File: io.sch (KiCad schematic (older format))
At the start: 13 parts, among them J5 USB_C_Receptacle_USB2.0, J6 Conn_ARM_JTAG_SWD_10, J7 UART, J8 Conn_02x14_Odd_Even

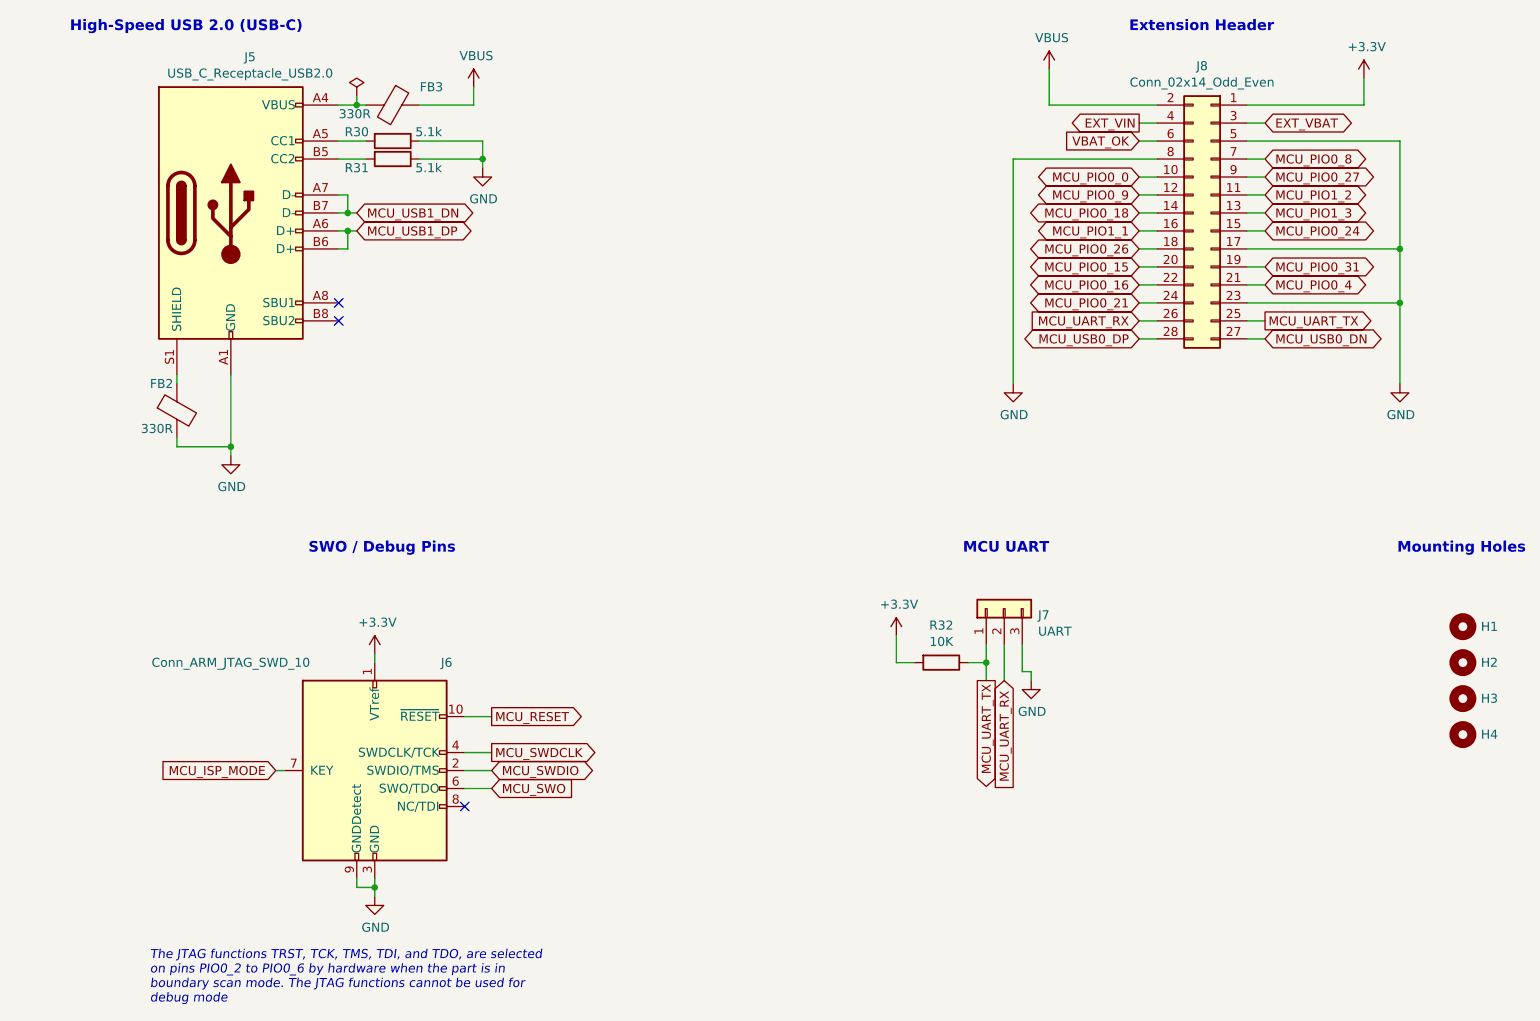
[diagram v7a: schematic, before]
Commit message: Major change of the layout (reviewed) for V1.1
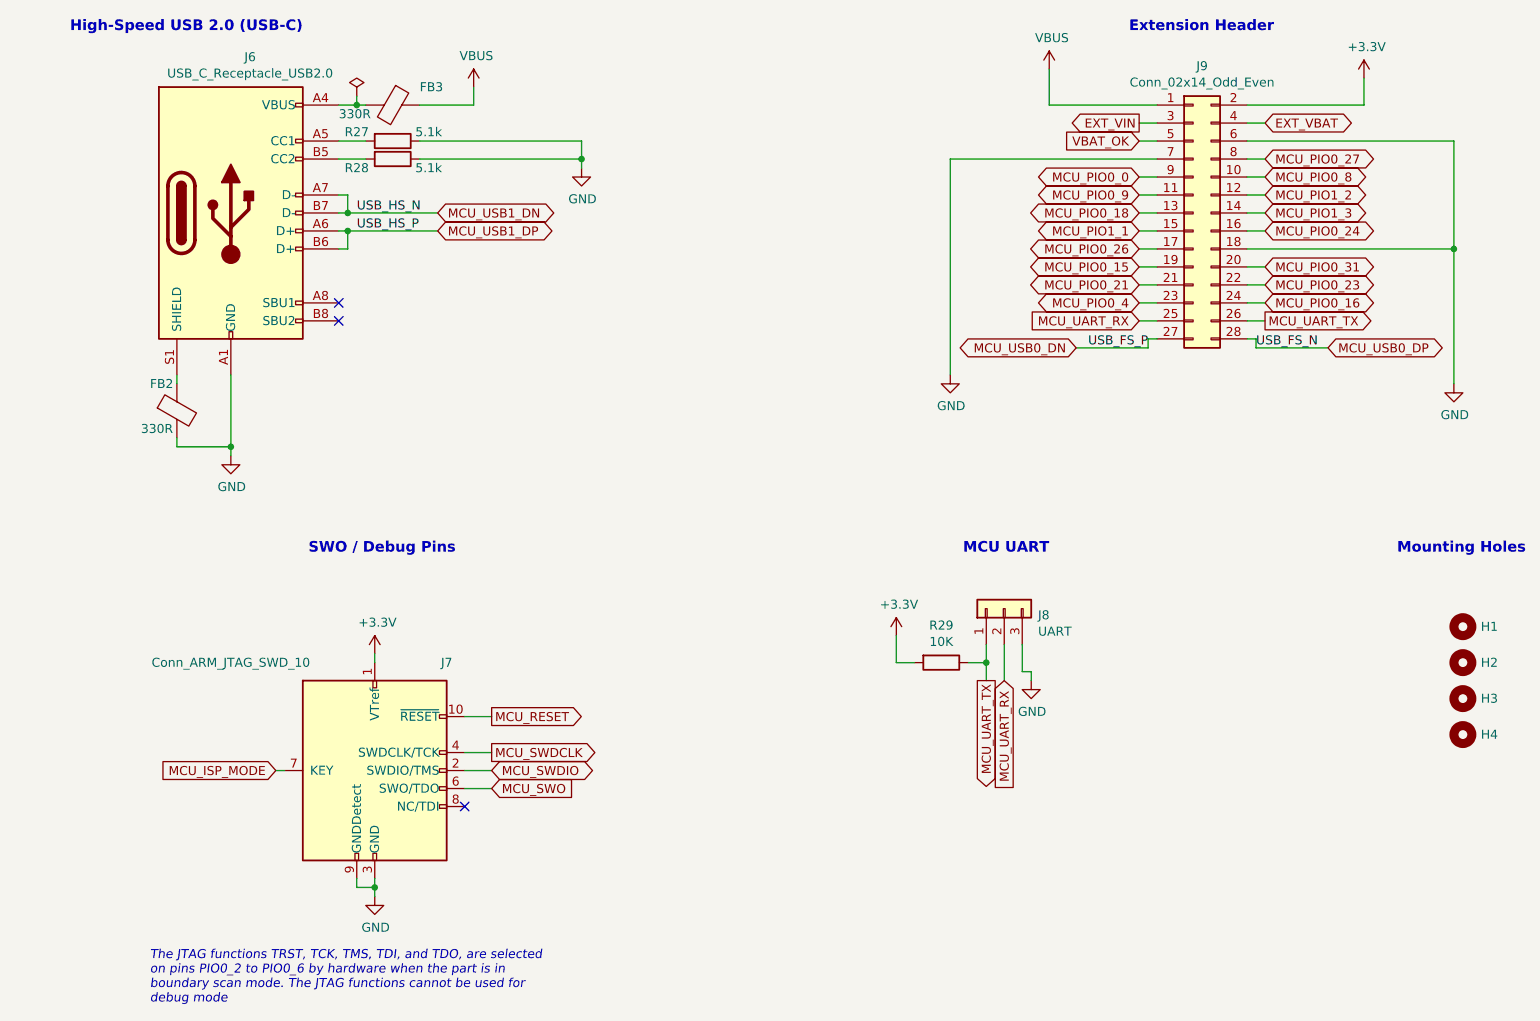
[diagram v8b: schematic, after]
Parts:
- renumbered J5 to J6, J6 to J7, J7 to J8, J8 to J9, R30 to R27, R31 to R28, R32 to R29
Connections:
- net +3V3: now also J9.2 (Pin_2); no longer J9.1 (Pin_1)
- net EXT_VBAT: now also J9.4 (Pin_4); no longer J9.3 (Pin_3)
- net EXT_VIN: now also J9.3 (Pin_3); no longer J9.4 (Pin_4)
- net GND: now also J9.18 (Pin_18), J9.6 (Pin_6), J9.7 (Pin_7); no longer J9.17 (Pin_17), J9.23 (Pin_23), J9.5 (Pin_5), J9.8 (Pin_8)
- net MCU_PIO0_0: now also J9.9 (Pin_9); no longer J9.10 (Pin_10)
- net MCU_PIO0_15: now also J9.19 (Pin_19); no longer J9.20 (Pin_20)
- net MCU_PIO0_16: now also J9.24 (Pin_24); no longer J9.22 (Pin_22)
- net MCU_PIO0_18: now also J9.13 (Pin_13); no longer J9.14 (Pin_14)
- net MCU_PIO0_21: now also J9.21 (Pin_21); no longer J9.24 (Pin_24)
- net MCU_PIO0_24: now also J9.16 (Pin_16); no longer J9.15 (Pin_15)
- net MCU_PIO0_26: now also J9.17 (Pin_17); no longer J9.18 (Pin_18)
- net MCU_PIO0_27: now also J9.8 (Pin_8); no longer J9.9 (Pin_9)
- net MCU_PIO0_31: now also J9.20 (Pin_20); no longer J9.19 (Pin_19)
- net MCU_PIO0_4: now also J9.23 (Pin_23); no longer J9.21 (Pin_21)
- net MCU_PIO0_8: now also J9.10 (Pin_10); no longer J9.7 (Pin_7)
- net MCU_PIO0_9: now also J9.11 (Pin_11); no longer J9.12 (Pin_12)
- net MCU_PIO1_1: now also J9.15 (Pin_15); no longer J9.16 (Pin_16)
- net MCU_PIO1_2: now also J9.12 (Pin_12); no longer J9.11 (Pin_11)
- net MCU_PIO1_3: now also J9.14 (Pin_14); no longer J9.13 (Pin_13)
- net MCU_UART_RX: now also J9.25 (Pin_25); no longer J9.26 (Pin_26)
- net MCU_UART_TX: now also J9.26 (Pin_26); no longer J9.25 (Pin_25)
- net VBAT_OK: now also J9.5 (Pin_5); no longer J9.6 (Pin_6)
- net VBUS: now also J9.1 (Pin_1); no longer J9.2 (Pin_2)
- new net MCU_PIO0_23: J9.22 (Pin_22)
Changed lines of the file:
@@
 Comment4 ""
 $EndDescr
-Text GLabel 3350 2200 2    50   BiDi ~ 0
+Text GLabel 3800 2200 2    50   BiDi ~ 0
 MCU_USB1_DN
 $Comp
-L Connector:USB_C_Receptacle_USB2.0 J5
+L Connector:USB_C_Receptacle_USB2.0 J6
 U 1 1 5F8BDC65
 P 2650 2200
-F 0 "J5" H 2757 3067 50  0000 C CNN
+F 0 "J6" H 2757 3067 50  0000 C CNN
 F 1 "USB_C_Receptacle_USB2.0" H 2757 2976 50  0000 C CNN
 F 2 "tardigrade-components:USB_C_Receptacle_JAE_DX07S016JA1" H 2800 2200 50  0001 C CNN
@@
 	1    0    0    -1
 $EndComp
-Text GLabel 3350 2300 2    50   BiDi ~ 0
+Text GLabel 3800 2300 2    50   BiDi ~ 0
 MCU_USB1_DP
 $Comp
@@
 	2350 3100 2350 3150
 $Comp
-L power:GND #PWR066
+L power:GND #PWR064
 U 1 1 5F8C3DD9
 P 2650 3550
-F 0 "#PWR066" H 2650 3300 50  0001 C CNN
+F 0 "#PWR064" H 2650 3300 50  0001 C CNN
 F 1 "GND" H 2655 3377 50  0000 C CNN
 F 2 "" H 2650 3550 50  0001 C CNN
@@
 NoConn ~ 3250 2800
 $Comp
-L Device:R R31
+L Device:R R28
 U 1 1 5F8C970D
 P 3550 1900
-F 0 "R31" V 3600 1700 50  0000 C CNN
+F 0 "R28" V 3600 1700 50  0000 C CNN
 F 1 "5.1k" V 3600 2100 50  0000 C CNN
 F 2 "Resistor_SMD:R_0402_1005Metric" V 3480 1900 50  0001 C CNN
@@
 $EndComp
 $Comp
-L Device:R R30
+L Device:R R27
 U 1 1 5F8CA21C
 P 3550 1800
-F 0 "R30" V 3500 1600 50  0000 C CNN
+F 0 "R27" V 3500 1600 50  0000 C CNN
 F 1 "5.1k" V 3500 2000 50  0000 C CNN
 F 2 "Resistor_SMD:R_0402_1005Metric" V 3480 1800 50  0001 C CNN
@@
 	3250 1900 3400 1900
 $Comp
-L power:GND #PWR070
+L power:GND #PWR068
 U 1 1 5F8CB237
-P 4050 1950
-F 0 "#PWR070" H 4050 1700 50  0001 C CNN
-F 1 "GND" H 4055 1777 50  0000 C CNN
-F 2 "" H 4050 1950 50  0001 C CNN
-F 3 "" H 4050 1950 50  0001 C CNN
-	1    4050 1950
-	1    0    0    -1
-$EndComp
-Wire Wire Line
-	3700 1900 4050 1900
-Wire Wire Line
-	4050 1900 4050 1950
-Wire Wire Line
-	3700 1800 4050 1800
-Wire Wire Line
-	4050 1800 4050 1900
-Connection ~ 4050 1900
-$Comp
-L power:VBUS #PWR069
+P 4600 1950
+F 0 "#PWR068" H 4600 1700 50  0001 C CNN
+F 1 "GND" H 4605 1777 50  0000 C CNN
+F 2 "" H 4600 1950 50  0001 C CNN
+F 3 "" H 4600 1950 50  0001 C CNN
+	1    4600 1950
+	1    0    0    -1
+$EndComp
+Wire Wire Line
+	3700 1900 4600 1900
+Wire Wire Line
+	4600 1900 4600 1950
+Wire Wire Line
+	3700 1800 4600 1800
+Wire Wire Line
+	4600 1800 4600 1900
+Connection ~ 4600 1900
+$Comp
+L power:VBUS #PWR067
 U 1 1 5F8C64F0
 P 4000 1500
-F 0 "#PWR069" H 4000 1350 50  0001 C CNN
+F 0 "#PWR067" H 4000 1350 50  0001 C CNN
 F 1 "VBUS" H 4015 1673 50  0000 C CNN
 F 2 "" H 4000 1500 50  0001 C CNN
@@
 NoConn ~ 3950 5500
 $Comp
-L power:GND #PWR068
+L power:GND #PWR066
 U 1 1 5FB23809
 P 3450 6000
-F 0 "#PWR068" H 3450 5750 50  0001 C CNN
+F 0 "#PWR066" H 3450 5750 50  0001 C CNN
 F 1 "GND" H 3455 5827 50  0000 C CNN
 F 2 "" H 3450 6000 50  0001 C CNN
@@
 	3450 6000 3450 5950
 $Comp
-L tardigrade-components:Conn_ARM_JTAG_SWD_10 J6
+L tardigrade-components:Conn_ARM_JTAG_SWD_10 J7
 U 1 1 5FB2D29C
 P 3450 5300
-F 0 "J6" H 3850 5900 50  0000 C CNN
+F 0 "J7" H 3850 5900 50  0000 C CNN
 F 1 "Conn_ARM_JTAG_SWD_10" H 2650 5900 50  0000 C CNN
 F 2 "Connector_PinHeader_1.27mm:PinHeader_2x05_P1.27mm_Vertical" H 3450 5300 50  0001 C CNN
@@
 High-Speed USB 2.0 (USB-C)
 $Comp
-L Connector_Generic:Conn_01x03 J7
+L Connector_Generic:Conn_01x03 J8
 U 1 1 5F876392
 P 6950 4400
-F 0 "J7" V 6914 4212 50  0000 R CNN
+F 0 "J8" V 6914 4212 50  0000 R CNN
 F 1 "UART" V 6823 4212 50  0000 R CNN
 F 2 "Connector_PinHeader_2.54mm:PinHeader_1x03_P2.54mm_Vertical" H 6950 4400 50  0001 C CNN
@@
 MCU_UART_TX
 $Comp
-L power:GND #PWR073
+L power:GND #PWR071
 U 1 1 5F877DE3
 P 7100 4800
-F 0 "#PWR073" H 7100 4550 50  0001 C CNN
+F 0 "#PWR071" H 7100 4550 50  0001 C CNN
 F 1 "GND" H 7105 4627 50  0000 C CNN
 F 2 "" H 7100 4800 50  0001 C CNN
@@
 	7100 4750 7100 4800
 $Comp
-L power:+3.3V #PWR071
+L power:+3.3V #PWR069
 U 1 1 5F8E0D6F
 P 6350 4550
-F 0 "#PWR071" H 6350 4400 50  0001 C CNN
+F 0 "#PWR069" H 6350 4400 50  0001 C CNN
 F 1 "+3.3V" H 6365 4723 50  0000 C CNN
 F 2 "" H 6350 4550 50  0001 C CNN
@@
 $EndComp
 $Comp
-L Device:R R32
+L Device:R R29
 U 1 1 5F8E1A3D
 P 6600 4700
-F 0 "R32" V 6393 4700 50  0000 C CNN
+F 0 "R29" V 6393 4700 50  0000 C CNN
 F 1 "10K" V 6484 4700 50  0000 C CNN
 F 2 "Resistor_SMD:R_0402_1005Metric" V 6530 4700 50  0001 C CNN
@@
 	3250 2300 3300 2300
 $Comp
-L power:+3.3V #PWR067
+L power:+3.3V #PWR065
 U 1 1 5F833987
 P 3450 4650
-F 0 "#PWR067" H 3450 4500 50  0001 C CNN
+F 0 "#PWR065" H 3450 4500 50  0001 C CNN
 F 1 "+3.3V" H 3465 4823 50  0000 C CNN
 F 2 "" H 3450 4650 50  0001 C CNN
@@
 Connection ~ 3300 2200
 Wire Wire Line
-	3300 2200 3350 2200
+	3300 2200 3800 2200
 Wire Wire Line
 	3300 2400 3300 2300
 Connection ~ 3300 2300
 Wire Wire Line
-	3300 2300 3350 2300
+	3300 2300 3800 2300
 Wire Wire Line
 	3700 1600 4000 1600
@@
 	3350 1600 3350 1550
 $Comp
-L power:PWR_FLAG #FLG08
+L power:PWR_FLAG #FLG06
 U 1 1 5FCB5DBF
 P 3350 1550
-F 0 "#FLG08" H 3350 1625 50  0001 C CNN
+F 0 "#FLG06" H 3350 1625 50  0001 C CNN
 F 1 "PWR_FLAG" H 3350 1723 50  0001 C CNN
 F 2 "" H 3350 1550 50  0001 C CNN
@@
 Wire Wire Line
 	3450 4650 3450 4700
-$Comp
-L Connector_Generic:Conn_02x14_Odd_Even J8
-U 1 1 5FAF0C03
-P 8100 2200
-F 0 "J8" H 8150 3017 50  0000 C CNN
-F 1 "Conn_02x14_Odd_Even" H 8150 2926 50  0000 C CNN
-F 2 "Connector_PinHeader_2.54mm:PinHeader_2x14_P2.54mm_Vertical" H 8100 2200 50  0001 C CNN
-F 3 "~" H 8100 2200 50  0001 C CNN
-	1    8100 2200
-	-1   0    0    -1
-$EndComp
 Text GLabel 8400 1700 2    50   BiDi ~ 0
 EXT_VBAT
@@
 VBAT_OK
 $Comp
-L power:VBUS #PWR0110
+L power:VBUS #PWR072
 U 1 1 5FB21530
 P 7200 1400
-F 0 "#PWR0110" H 7200 1250 50  0001 C CNN
+F 0 "#PWR072" H 7200 1250 50  0001 C CNN
 F 1 "VBUS" H 7215 1573 50  0000 C CNN
 F 2 "" H 7200 1400 50  0001 C CNN
@@
 	7200 1600 7800 1600
 $Comp
-L power:+3.3V #PWR0111
+L power:+3.3V #PWR073
 U 1 1 5FB24107
 P 8950 1450
-F 0 "#PWR0111" H 8950 1300 50  0001 C CNN
+F 0 "#PWR073" H 8950 1300 50  0001 C CNN
 F 1 "+3.3V" H 8965 1623 50  0000 C CNN
 F 2 "" H 8950 1450 50  0001 C CNN
@@
 $EndComp
 Wire Wire Line
-	8300 1600 8950 1600
-Wire Wire Line
 	8950 1600 8950 1450
-Text GLabel 8400 2900 2    50   BiDi ~ 0
+Text GLabel 7350 2950 0    50   BiDi ~ 0
 MCU_USB0_DN
-Text GLabel 7700 2900 0    50   BiDi ~ 0
+Text GLabel 8750 2950 2    50   BiDi ~ 0
 MCU_USB0_DP
 Text GLabel 8400 2800 2    50   Output ~ 0
@@
 Text GLabel 7700 2800 0    50   Input ~ 0
 MCU_UART_RX
-Text GLabel 8400 2600 2    50   BiDi ~ 0
+Text GLabel 7700 2700 0    50   BiDi ~ 0
 MCU_PIO0_4
-Text GLabel 7700 2700 0    50   BiDi ~ 0
+Text GLabel 7700 2600 0    50   BiDi ~ 0
 MCU_PIO0_21
-Text GLabel 7700 2600 0    50   BiDi ~ 0
+Text GLabel 8400 2700 2    50   BiDi ~ 0
 MCU_PIO0_16
 Text GLabel 7700 2500 0    50   BiDi ~ 0
@@
 Text GLabel 7700 2000 0    50   BiDi ~ 0
 MCU_PIO0_0
+Text GLabel 8400 2000 2    50   BiDi ~ 0
+MCU_PIO0_8
 Text GLabel 8400 1900 2    50   BiDi ~ 0
-MCU_PIO0_8
-Text GLabel 8400 2000 2    50   BiDi ~ 0
 MCU_PIO0_27
 $Comp
-L power:GND #PWR0108
+L power:GND #PWR074
 U 1 1 5FCCD42F
-P 9150 3150
-F 0 "#PWR0108" H 9150 2900 50  0001 C CNN
-F 1 "GND" H 9155 2977 50  0000 C CNN
-F 2 "" H 9150 3150 50  0001 C CNN
-F 3 "" H 9150 3150 50  0001 C CNN
-	1    9150 3150
-	1    0    0    -1
-$EndComp
-$Comp
-L power:GND #PWR0109
+P 9450 3150
+F 0 "#PWR074" H 9450 2900 50  0001 C CNN
+F 1 "GND" H 9455 2977 50  0000 C CNN
+F 2 "" H 9450 3150 50  0001 C CNN
+F 3 "" H 9450 3150 50  0001 C CNN
+	1    9450 3150
+	1    0    0    -1
+$EndComp
+$Comp
+L power:GND #PWR070
 U 1 1 5FCCD82E
-P 7000 3150
-F 0 "#PWR0109" H 7000 2900 50  0001 C CNN
-F 1 "GND" H 7005 2977 50  0000 C CNN
-F 2 "" H 7000 3150 50  0001 C CNN
-F 3 "" H 7000 3150 50  0001 C CNN
-	1    7000 3150
-	1    0    0    -1
-$EndComp
-Wire Wire Line
-	7000 3150 7000 1900
-Wire Wire Line
-	7000 1900 7800 1900
-Wire Wire Line
-	8300 1800 9150 1800
-Wire Wire Line
-	9150 1800 9150 2400
-Wire Wire Line
-	8300 2400 9150 2400
-Connection ~ 9150 2400
-Wire Wire Line
-	9150 2400 9150 2700
-Wire Wire Line
-	8300 2700 9150 2700
-Connection ~ 9150 2700
-Wire Wire Line
-	9150 2700 9150 3150
+P 6650 3100
+F 0 "#PWR070" H 6650 2850 50  0001 C CNN
+F 1 "GND" H 6655 2927 50  0000 C CNN
+F 2 "" H 6650 3100 50  0001 C CNN
+F 3 "" H 6650 3100 50  0001 C CNN
+	1    6650 3100
+	1    0    0    -1
+$EndComp
+Wire Wire Line
+	6650 3100 6650 1900
+Wire Wire Line
+	6650 1900 7800 1900
+Wire Wire Line
+	9450 1800 9450 2400
+Connection ~ 9450 2400
 Wire Wire Line
 	7700 1700 7800 1700
@@
 	7700 2800 7800 2800
 Wire Wire Line
-	7800 2900 7700 2900
-Wire Wire Line
-	8300 2900 8400 2900
-Wire Wire Line
 	8400 2800 8300 2800
 Wire Wire Line
@@
 Wire Wire Line
 	8300 1700 8400 1700
+Wire Wire Line
+	9450 2400 9450 3150
+Text GLabel 8400 2600 2    50   BiDi ~ 0
+MCU_PIO0_23
+Wire Wire Line
+	8300 2700 8400 2700
+$Comp
+L Connector_Generic:Conn_02x14_Odd_Even J9
+U 1 1 5FAF0C03
+P 8000 2200
+F 0 "J9" H 8050 3017 50  0000 C CNN
+F 1 "Conn_02x14_Odd_Even" H 8050 2926 50  0000 C CNN
+F 2 "Connector_PinHeader_2.54mm:PinHeader_2x14_P2.54mm_Vertical" H 8000 2200 50  0001 C CNN
+F 3 "~" H 8000 2200 50  0001 C CNN
+	1    8000 2200
+	1    0    0    -1
+$EndComp
+Wire Wire Line
+	8300 1600 8950 1600
+Wire Wire Line
+	8300 1800 9450 1800
+Wire Wire Line
+	8300 2400 9450 2400
+Text Label 3350 2200 0    50   ~ 0
+USB_HS_N
+Text Label 3350 2300 0    50   ~ 0
+USB_HS_P
+Text Label 7750 2950 2    50   ~ 0
+USB_FS_P
+Wire Wire Line
+	7800 2900 7750 2900
+Wire Wire Line
+	7750 2900 7750 2950
+Wire Wire Line
+	7750 2950 7350 2950
+Wire Wire Line
+	8300 2900 8350 2900
+Wire Wire Line
+	8350 2900 8350 2950
+Wire Wire Line
+	8350 2950 8750 2950
+Text Label 8350 2950 0    50   ~ 0
+USB_FS_N
 $EndSCHEMATC
